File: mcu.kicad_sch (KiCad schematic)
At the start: 65 parts, among them J1 USB_C, P20 HEADER-2x11, P22 HEADER-2x13, P26 LPC_JTAG, P28 HEADER-2x11, SW1 SWITCH, SW2 SWITCH, U15 TVS_USB, U20 W25Q80, U23 LPC4330FET180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

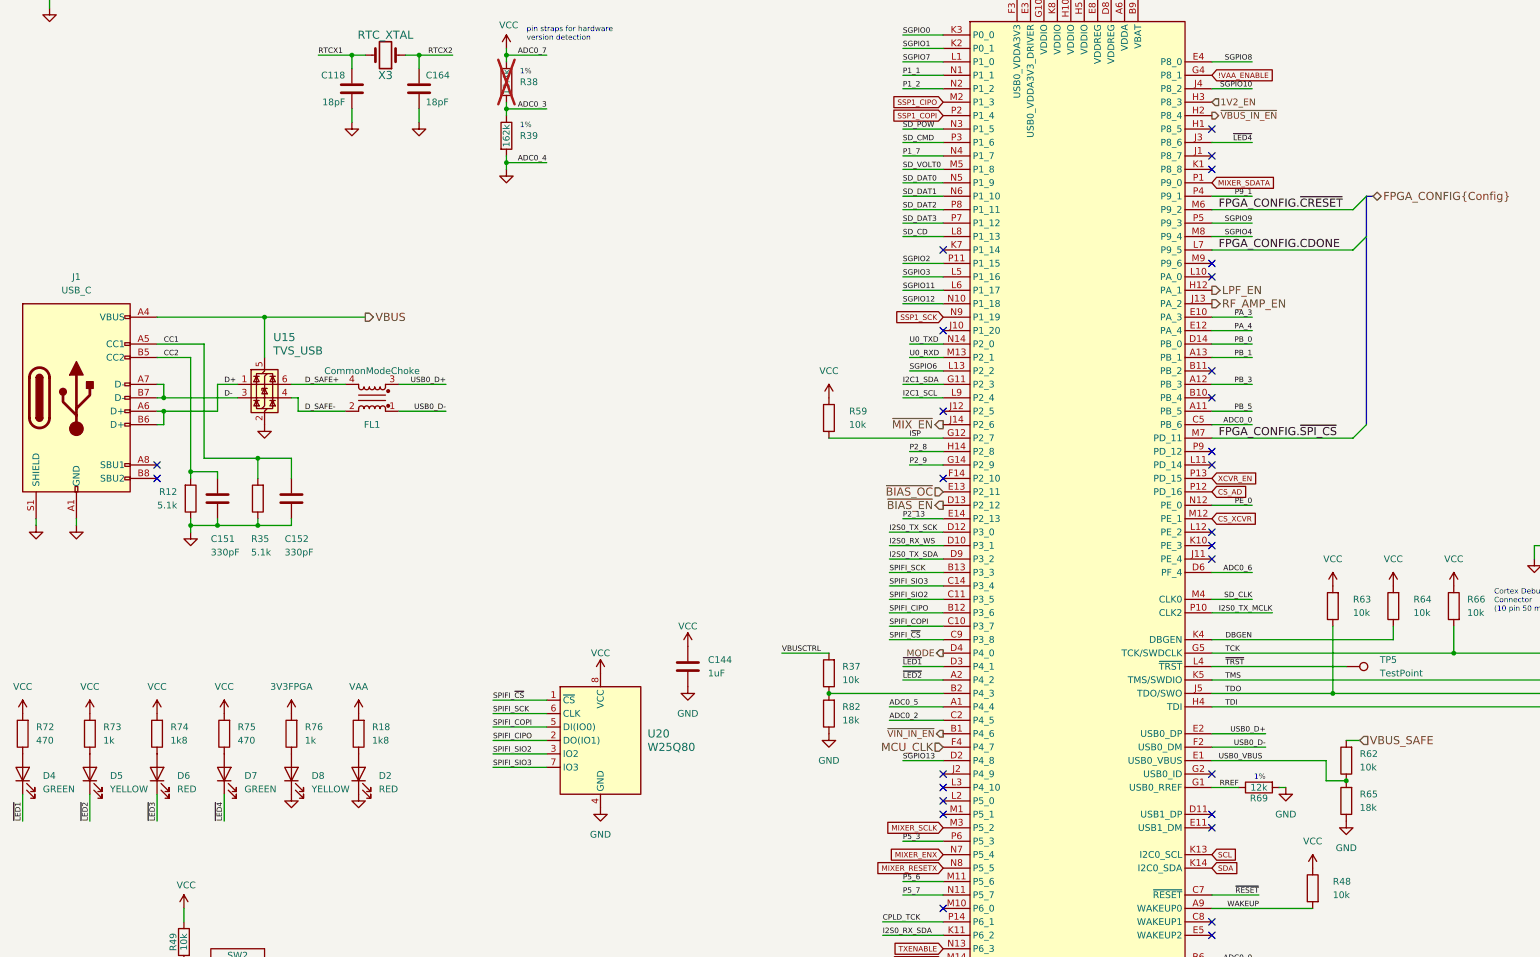
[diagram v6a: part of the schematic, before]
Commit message: Add Type-C controller
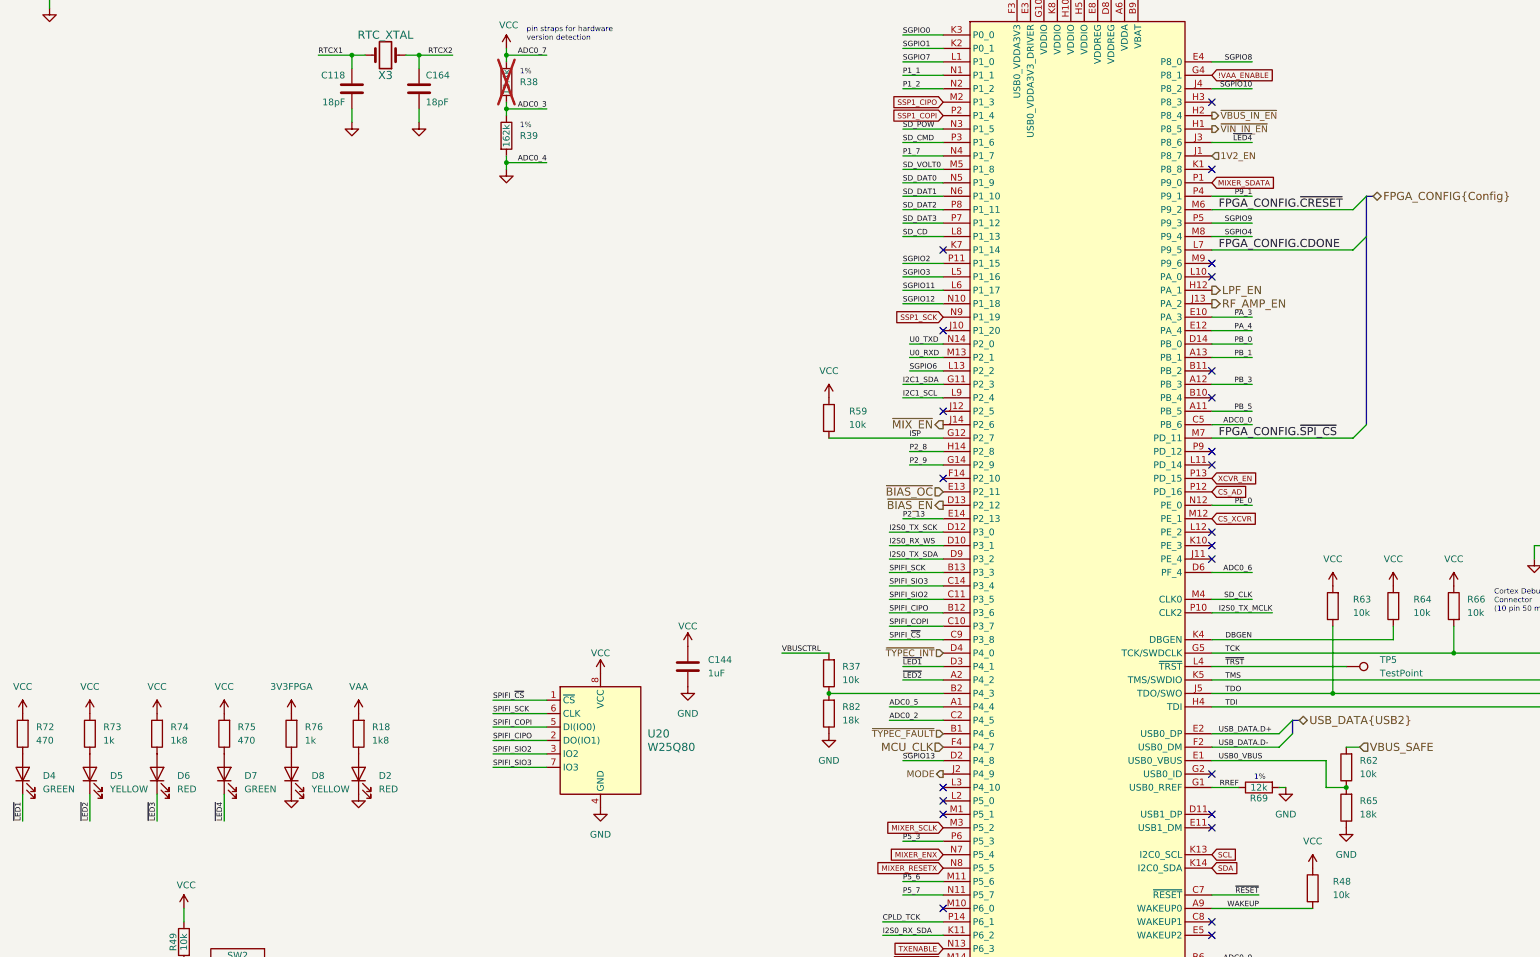
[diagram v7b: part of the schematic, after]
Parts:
- removed C151, C152: 330pF, Capacitor_SMD:C_0201_0603Metric, symbol Device:C
- removed FL1: CommonModeChoke, praline:L_CommonModeChoke_Murata_DLM0NS, symbol Device:Filter_EMI_CommonMode
- removed J1: USB_C, praline:USB_C_Receptacle_HRO_TYPE-C-31-M-12, symbol Connector:USB_C_Receptacle_USB2.0_16P
- removed R12, R35: 5.1k, Resistor_SMD:R_0402_1005Metric, symbol Device:R
- removed U15: TVS_USB, Package_TO_SOT_SMD:SOT-563, symbol Power_Protection:USBLC6-2P6
- TP5: now left out of the parts list
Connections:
- net 1V2_EN: now also U23.J1 (P8_7); no longer U23.H3 (P8_3)
- net MODE: now also U23.J2 (P4_9); no longer U23.D4 (P4_0)
- net ~{VIN_IN_EN}: now also U23.H1 (P8_5); no longer U23.B1 (P4_6)
- net USB0_D+ renamed USB_DATA.D+
- net USB0_D- renamed USB_DATA.D-
- new net ~{TYPEC_FAULT}: U23.B1 (P4_6)
- new net ~{TYPEC_INT}: U23.D4 (P4_0)
- no-connect marks 34 -> 30
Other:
- moved on the sheet: R62, R65

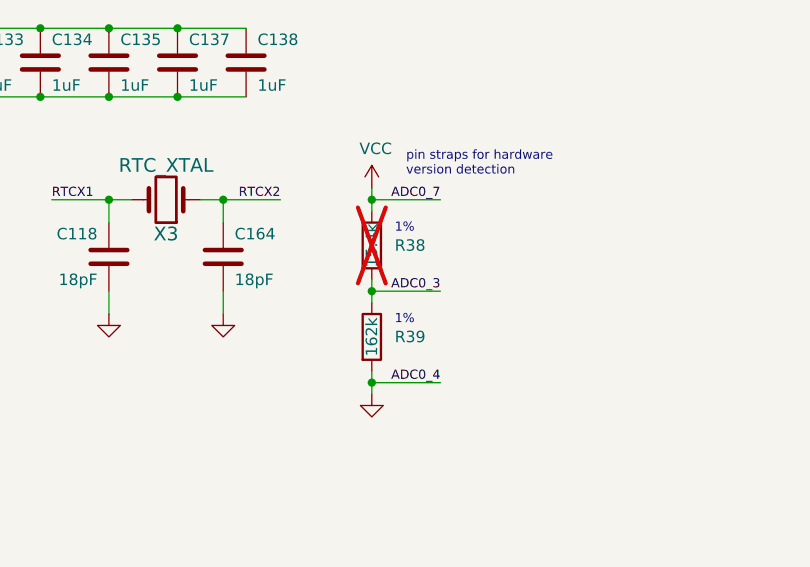
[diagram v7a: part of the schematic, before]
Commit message: Update hardware version detection pin strap
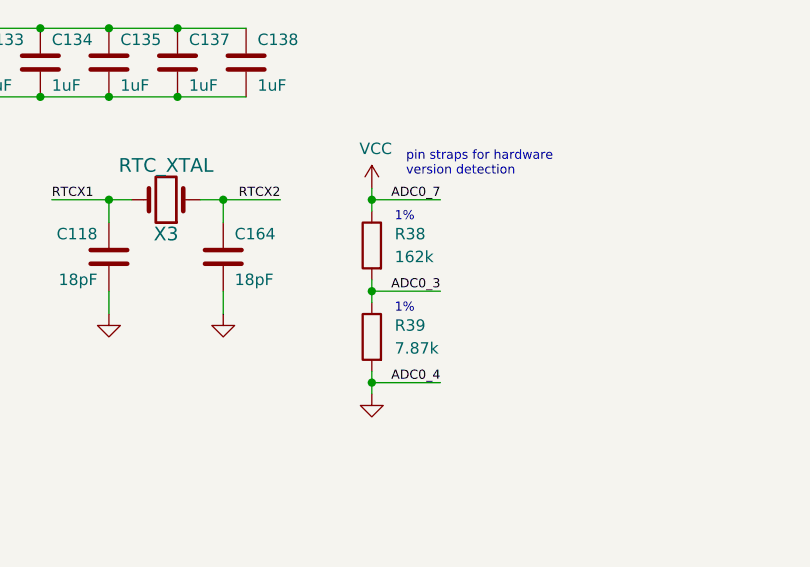
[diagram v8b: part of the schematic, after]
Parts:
- R38: value 15.4k -> 162k; Part Number RC0402FR-0715K4L -> RC0402FR-07162KL; now fitted
- R39: value 162k -> 7.87k; Part Number RC0402FR-07162KL -> RC0402FR-077K87L
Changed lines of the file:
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@@
 	(text "1%"
 		(exclude_from_sim no)
-		(at 114.3 53.34 0)
+		(at 114.3 52.07 0)
 		(effects
 			(font
@@
 	(text "1%"
 		(exclude_from_sim no)
-		(at 114.3 43.18 0)
+		(at 114.3 41.91 0)
 		(effects
 			(font
@@
 		(lib_id "Device:R")
 		(at 111.76 54.61 0)
+		(mirror y)
 		(unit 1)
 		(exclude_from_sim no)
@@
 		(dnp no)
 		(property "Reference" "R39"
-			(at 114.3 54.61 0)
+			(at 114.3 53.3399 0)
 			(effects
 				(font
 					(size 1.27 1.27)
 				)
-				(justify left)
+				(justify right)
 			)
 		)
-		(property "Value" "162k"
-			(at 111.76 54.61 90)
+		(property "Value" "7.87k"
+			(at 114.3 55.8799 0)
 			(effects
 				(font
 					(size 1.27 1.27)
 				)
+				(justify right)
 			)
 		)
@@
 			)
 		)
-		(property "Description" "RES 1/16W 162K OHM 1% 0402"
+		(property "Description" "RES 7.87K OHM 1% 1/16W 0402"
 			(at 111.76 54.61 0)
 			(effects
@@
 			)
 		)
-		(property "Part Number" "RC0402FR-07162KL"
+		(property "Part Number" "RC0402FR-077K87L"
 			(at 111.76 54.61 0)
 			(effects
@@
 		(lib_id "Device:R")
 		(at 111.76 44.45 0)
+		(mirror y)
 		(unit 1)
 		(exclude_from_sim no)
 		(in_bom yes)
 		(on_board yes)
-		(dnp yes)
+		(dnp no)
 		(property "Reference" "R38"
-			(at 114.3 44.45 0)
+			(at 114.3 43.1799 0)
 			(effects
 				(font
 					(size 1.27 1.27)
 				)
-				(justify left)
+				(justify right)
 			)
 		)
-		(property "Value" "15.4k"
-			(at 111.76 44.45 90)
+		(property "Value" "162k"
+			(at 114.3 45.7199 0)
 			(effects
 				(font
 					(size 1.27 1.27)
 				)
+				(justify right)
 			)
 		)
@@
 			)
 		)
-		(property "Description" "RES 15.4K OHM 1% 1/16W 0402"
+		(property "Description" "RES 1/16W 162K OHM 1% 0402"
 			(at 111.76 44.45 0)
 			(effects
@@
 			)
 		)
-		(property "Part Number" "RC0402FR-0715K4L"
+		(property "Part Number" "RC0402FR-07162KL"
 			(at 111.76 44.45 0)
 			(effects
